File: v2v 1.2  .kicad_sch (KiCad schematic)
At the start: 23 parts, among them J1 Conn_01x02, J2 USB_C_Receptacle_USB2.0_16P, U1 Ai-Thinker-Ra-01, U2 RXM-GPS-FM, U3 MPU-6050, U4 ESP32-C3-DevKitM-1, U5 ER_OLEDM0.91_1x-I2C, U6 MCP73123, U7 3V3_BUCK_BOOST, U8 Raspberry_Pi_5_Model_B

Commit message: Add Wokwi HIL simulation, fix pin map/nets, expose stack as MCP server
- firmware: remap to the ESP32-C3 schematic pins, drive buzzer/LED/OLED on
  alerts, emit bare JSON lines, transmit JSON lines received over USB serial,
  send relative TTL
- protocol: treat ttl/ts below 1e6 as relative/uptime values and rebase them
- schematic: unify +3V3/+3.3V and Bat+/BAT+, tie U7 EN to BAT+, add 330R
  series resistor for the LED on the +3.3V anode net
- wokwi: diagram, SX1278 and GPS NMEA custom chips (prebuilt WASM), PlatformIO
  envs, automation scenario
- hardware/sim: ngspice power-rail model and schematic netlist checker
- software/mcp_bridge.py: vision, fusion, mesh and cluster tools as an MCP
  server, registered with the Wokwi MCP server in .mcp.json
- hardware/run_hil.py and HIL_VERIFICATION.md: end-to-end run and report
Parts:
- added R5: 330, symbol Device:R
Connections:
- net +3V3 is gone; now on net +3.3V: C5.1, C6.1, U7.1 (VOUT), U7.10 (FB)
- net Bat+ is gone; now on net BAT+: J1.1 (Pin_1)
- net +3.3V: now also BZ1.1 (+), R5.1
- net BAT+: now also U7.6 (EN)
- net at D1.2 (A): now also R5.2; no longer BZ1.1 (+)

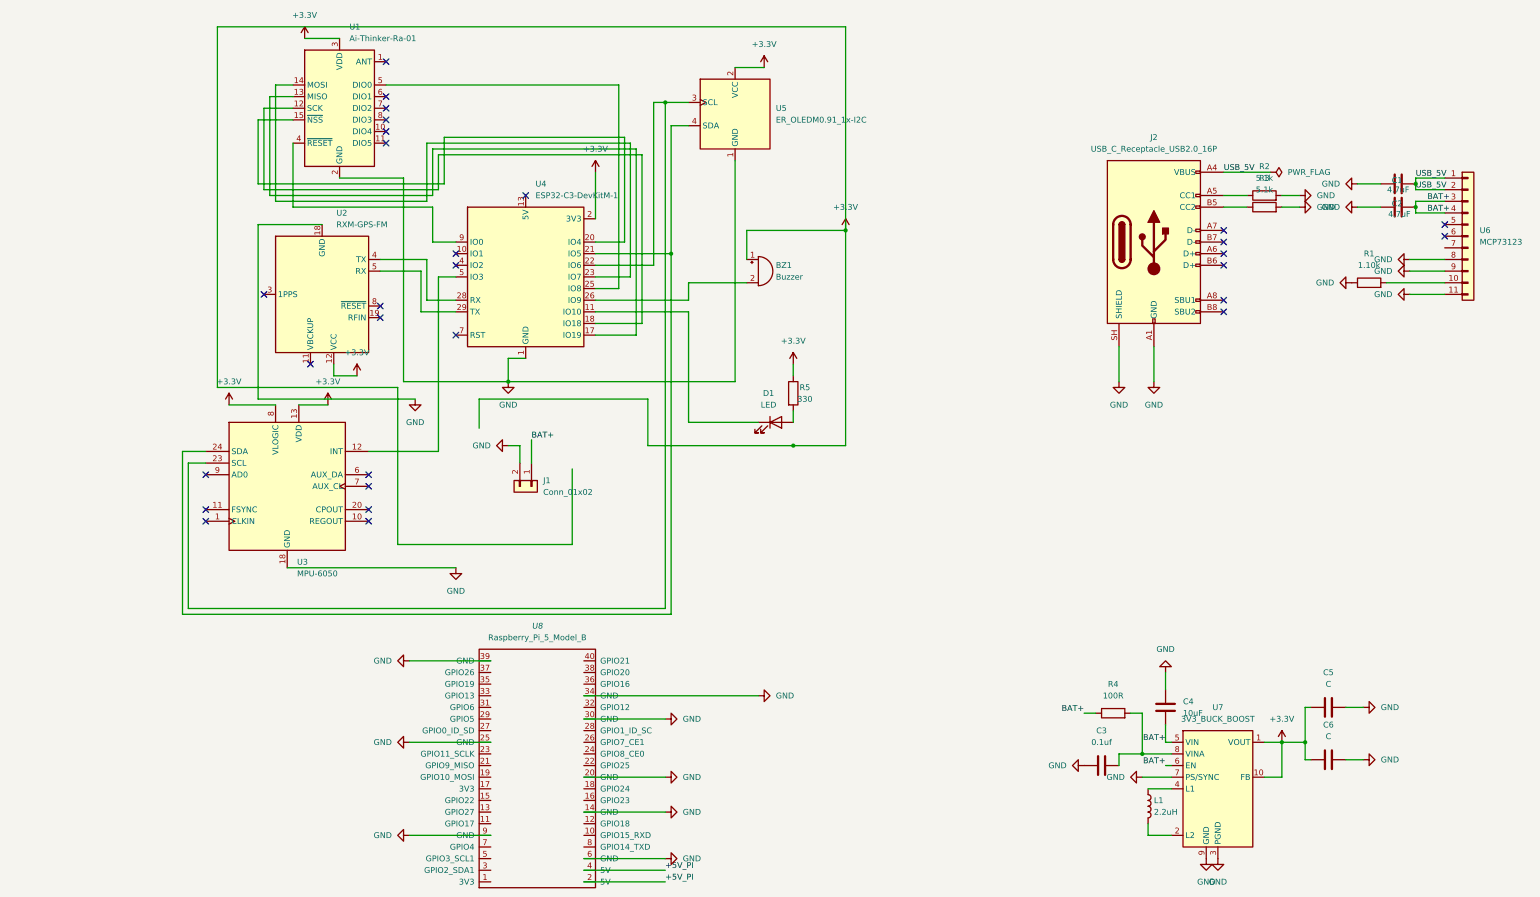
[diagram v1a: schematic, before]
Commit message: Fix GPS/USB pin clash, MPU6050 wiring and pothole emergency rule
- schematic/firmware: GPS UART moves to IO2 (RX) / IO1 (TX); IO20/IO21 stay
  the USB-UART console; drop the Wokwi-only USB-CDC build env
- schematic: tie MPU6050 AD0/FSYNC/CLKIN to GND, add REGOUT 0.1uF and CPOUT
  2.2nF caps plus 0.1uF bypass caps for U3 VDD/VLOGIC and U1 VDD
- emergency: pothole and crack clusters escalate as trusted hazards but never
  raise an EMERGENCY; debris/unknown hazards still do
- netlist_check: also join wire ends and pins that land on a wire interior
- mcp_bridge/run_hil: one emergency entry per logical packet, add a debris
  control case, parse the serial log without relying on newlines
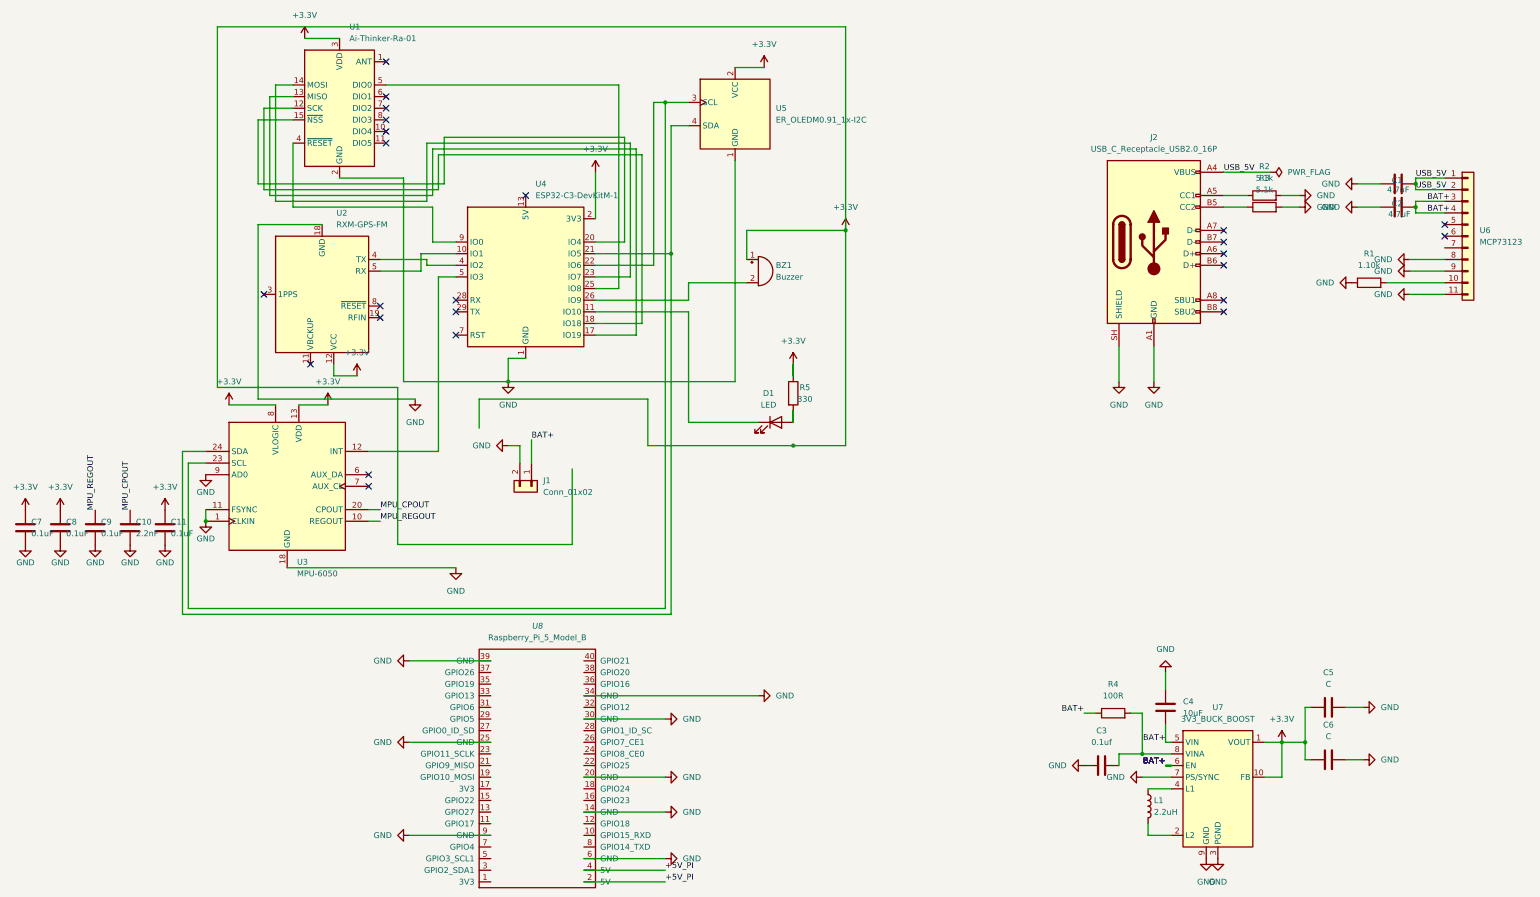
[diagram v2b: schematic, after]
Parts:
- added C10: 2.2nF, symbol Device:C
- added C11, C7, C8, C9: 0.1uF, symbol Device:C
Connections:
- net +3.3V: now also C11.1, C7.1, C8.1
- net GND: now also U3.1 (CLKIN), U3.11 (FSYNC), U3.9 (AD0), C10.2, C11.2, C7.2, C8.2, C9.2
- net at U2.4 (TX): now also U4.4 (IO2); no longer U4.28 (RX)
- net at U2.5 (RX): now also U4.10 (IO1); no longer U4.29 (TX)
- net MPU_REGOUT: now reaches U3.10 (REGOUT)
- net MPU_REGOUT: now also C9.1
- net MPU_CPOUT: now reaches U3.20 (CPOUT)
- net MPU_CPOUT: now also C10.1
- no-connect marks 29 -> 24

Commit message: Add push-to-talk voice over LoRa and clean up the schematic with KiCad CLI
- voice: Codec2 700C PTT (software/voice) with chunked VoicePacket frames,
  re-ordering receiver with loss concealment, half-duplex controller, talk
  limit, Pi node with GPIO button and I2S mic/speaker back ends; not relayed
- protocol/lora_node: VOICE packet type and voice callback, kept apart from
  the hazard pipeline
- firmware: voice lines pass through the ESP32 modem without buzzer/LED,
  OLED shows VOICE TX/RX, lines over one LoRa frame are refused
- schematic: PTT button, I2S mic and amp headers on the Pi header; ERC fixes
  (no-connect flags, PWR_FLAGs, grid alignment, dead wire branch removed)
- hardware/kicad_check.py: ERC and net assertions through kicad-cli 10
- mcp_bridge/run_hil: ptt_talk/ptt_state tools, time-on-air from the LoRa
  formula, Wokwi PTT scenario and 18 end-to-end checks
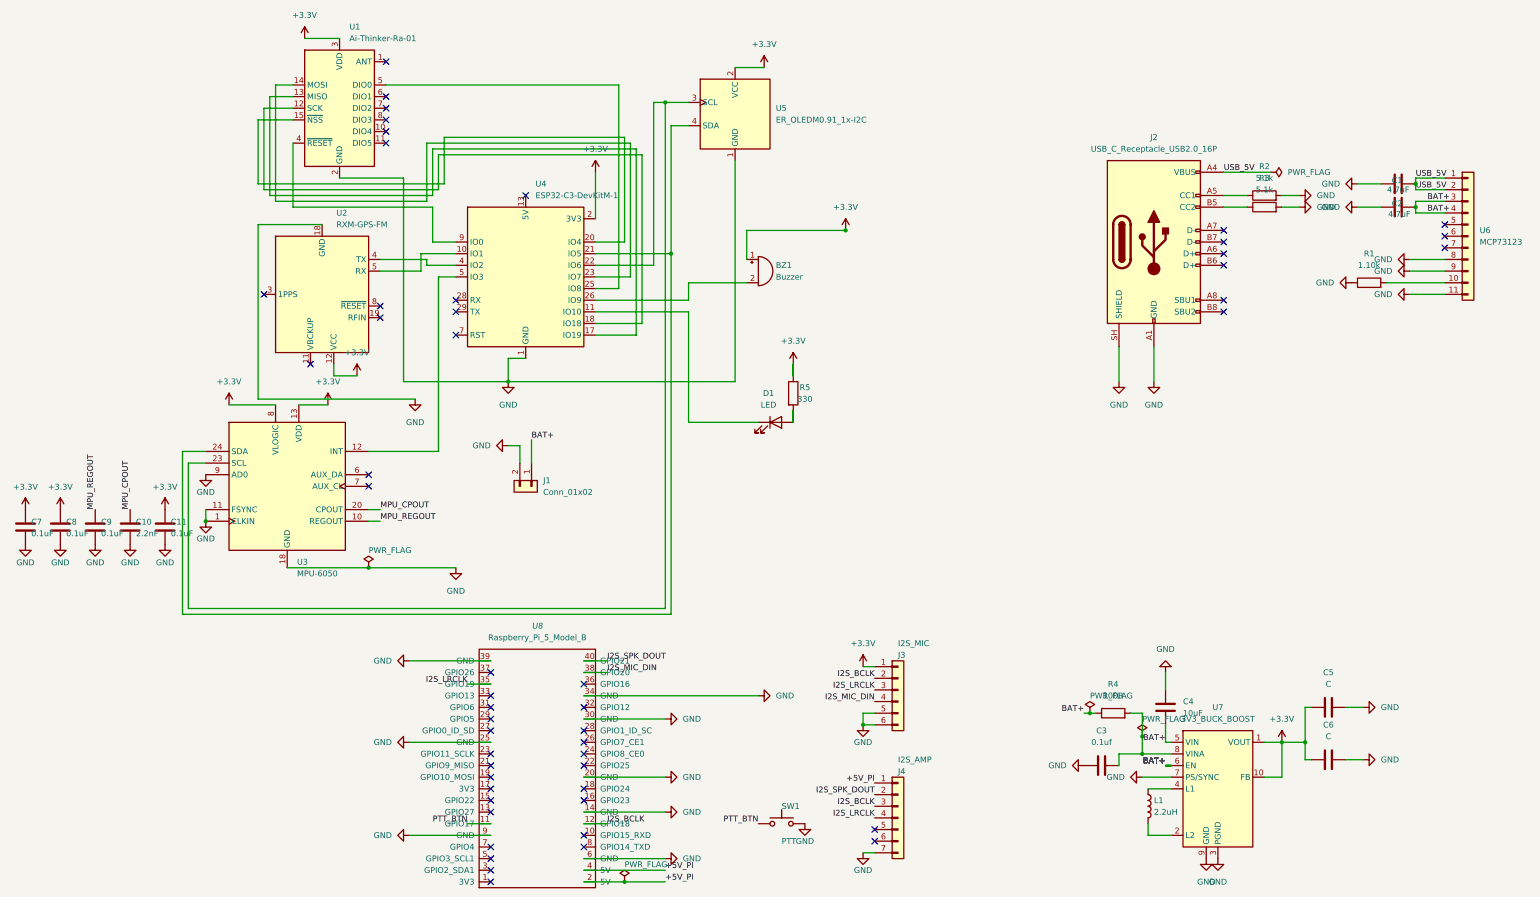
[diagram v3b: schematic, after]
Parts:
- added J3: I2S_MIC, symbol Connector_Generic:Conn_01x06
- added J4: I2S_AMP, symbol Connector_Generic:Conn_01x07
- added SW1: PTT, symbol Switch:SW_Push
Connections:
- net +3.3V: now also J3.1 (Pin_1)
- net +5V_PI: now also J4.1 (Pin_1)
- net GND: now also J3.5 (Pin_5), J3.6 (Pin_6), J4.7 (Pin_7), SW1.2
- net PTT_BTN: now reaches U8.11 (GPIO17)
- net PTT_BTN: now also SW1.1
- net I2S_BCLK: now reaches U8.12 (GPIO18)
- net I2S_BCLK: now also J3.2 (Pin_2), J4.3 (Pin_3)
- net I2S_LRCLK: now reaches U8.35 (GPIO19)
- net I2S_LRCLK: now also J3.3 (Pin_3), J4.4 (Pin_4)
- net I2S_MIC_DIN: now reaches U8.38 (GPIO20)
- net I2S_MIC_DIN: now also J3.4 (Pin_4)
- net I2S_SPK_DOUT: now reaches U8.40 (GPIO21)
- net I2S_SPK_DOUT: now also J4.2 (Pin_2)
- no-connect marks 24 -> 52
